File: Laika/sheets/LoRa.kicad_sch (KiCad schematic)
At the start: 0 parts

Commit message: Created schematic for Reyax RYLR993 LoRa module
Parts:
- added C13, C14: 47u, symbol Device:C
- added C15: 0.1u, symbol Device:C
- added C16: 100p, symbol Device:C
- added D16, D17, D18: LED, symbol Device:LED
- added J7: Conn_Coaxial_Small, symbol Connector:Conn_Coaxial_Small
- added JP1: SolderJumper_2_Open, symbol Jumper:SolderJumper_2_Open
- added Q5, Q6, Q7: Q_NMOS, symbol Device:Q_NMOS
- added R22, R23, R24, R25, R26, R27: 1k, symbol Device:R
- added TP6, TP7, TP8: TestPoint, TestPoint:TestPoint_Pad_D1.0mm, symbol Connector:TestPoint
- added U5: Reyax RYL993, Reyax_LoRa:RYLR993, symbol Reyax_LoRa:RYLR993
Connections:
- new net: Q6.D, R26.1
- new net: D17.1 (K), R26.2
- new net: Q6.G, R23.2
- new net: D16.1 (K), R25.2
- new net: D18.1 (K), R27.2
- new net: JP1.2 (B), U5.18 (PB12)
- new net: Q7.G, R24.2
- new net: Q5.G, R22.2
- new net: Q5.D, R25.1
- new net: Q7.D, R27.1
- new net +3V3: C13.1, C14.1, C15.1, C16.1, D16.2 (A), D17.2 (A), D18.2 (A), U5.12 (VBAT), U5.13 (VDD), U5.14 (VDD), U5.15 (VDD)
- new net GND: C13.2, C14.2, C15.2, C16.2, J7.2 (Ext), JP1.1 (A), Q5.S, Q6.S, Q7.S, U5.1 (GND), U5.10 (GND), U5.11 (GND), U5.22 (GND), U5.23 (GND), U5.28 (GND), U5.32 (GND), U5.41 (GND), U5.42 (GND), U5.44 (GND), U5.7 (GND), U5.8 (GND), U5.9 (GND)
- new net LINK: R22.1, U5.21 (PA12)
- new net LORA_ANTENNA: J7.1 (In), U5.43 (RF)
- new net LORA_NRST: TP8.1, U5.26 (NRST)
- new net LORA_RX: U5.40 (PA3/RXD)
- new net LORA_SWCLK: TP7.1, U5.27 (PA14/JTCK-SWCLK)
- new net LORA_SWDIO: TP6.1, U5.24 (PA13/JTMS-SWDIO)
- new net LORA_TX: U5.39 (PA2/TXD)
- new net RF_RX_ACTIVE: R24.1, U5.19 (PA10)
- new net RF_TX_ACTIVE: R23.1, U5.20 (PA11)
- no-connect marks 0 -> 17
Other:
- note added: "Antenna"
- note added: "LoRa Module"
- note added: "SWD"
- note added: "U.FL Connector"

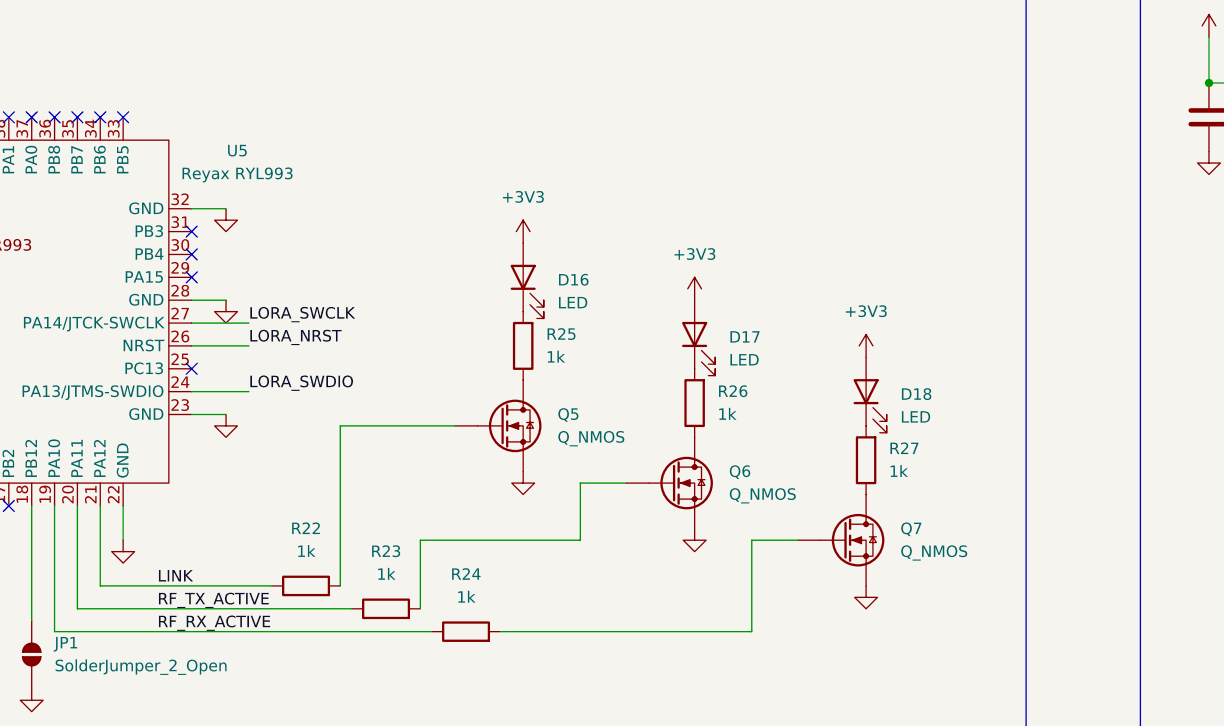
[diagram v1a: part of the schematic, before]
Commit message: Populated BOM with part numbers and footprints
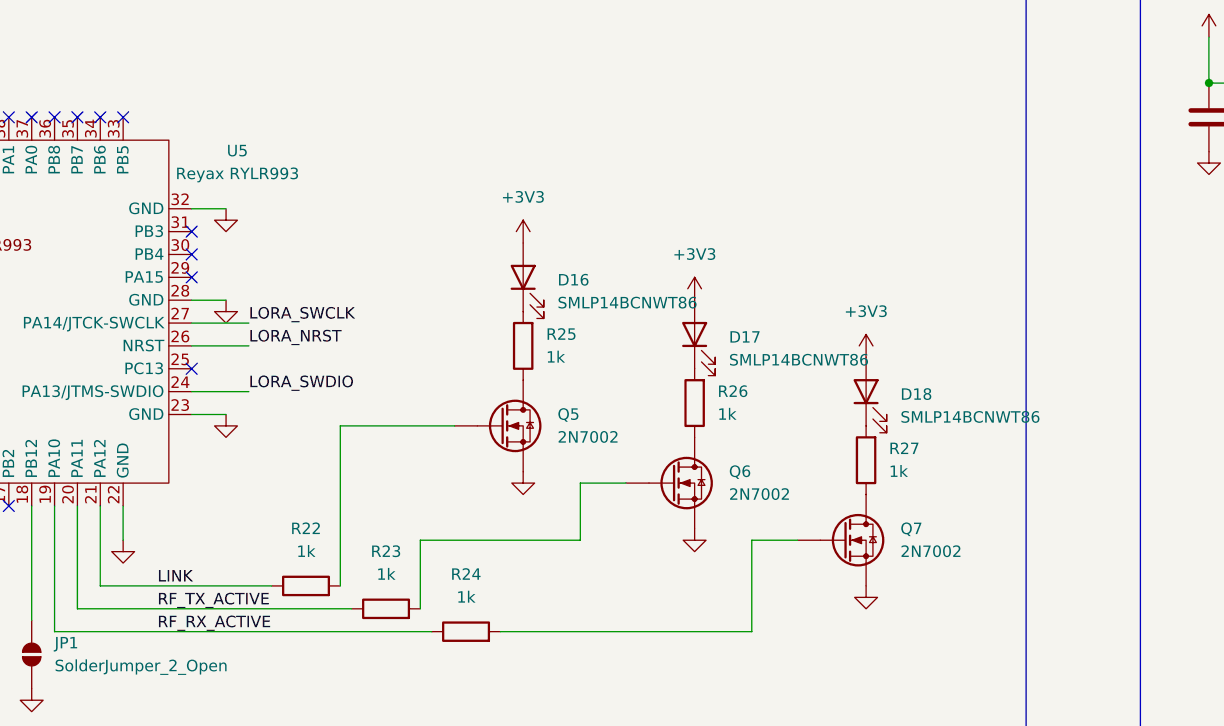
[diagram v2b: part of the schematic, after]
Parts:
- C13, C14: footprint (none) -> Capacitor_SMD:C_0805_2012Metric; JLC Part Type (none) -> Basic; Manafacturer (none) -> Samsung Electro-Mechanics; Part Number (none) -> CL21A476MQYNNNE
- C15: footprint (none) -> Capacitor_SMD:C_0402_1005Metric; JLC Part Type (none) -> Basic; Manafacturer (none) -> Samsung Electro-Mechanics; Part Number (none) -> CL05B104KO5NNNC
- C16: footprint (none) -> Capacitor_SMD:C_0201_0603Metric; JLC Part Type (none) -> Basic; Manafacturer (none) -> Samsung Electro-Mechanics; Part Number (none) -> CL10C101JB8NNNC
- D16, D17, D18: value LED -> SMLP14BCNWT86; footprint (none) -> LED_SMD:LED_0402_1005Metric; JLC Part Type (none) -> Extended; Manafacturer (none) -> Rohm Semiconductor; Part Number (none) -> SMLP14BCNWT86
- J7: footprint (none) -> Connector_Coaxial:U.FL_Molex_MCRF_73412-0110_Vertical; JLC Part Type (none) -> Extended; Manafacturer (none) -> Molex; Part Number (none) -> 0734120110
- JP1: footprint (none) -> Jumper:SolderJumper-2_P1.3mm_Open_Pad1.0x1.5mm
- Q5, Q6, Q7: value Q_NMOS -> 2N7002; footprint (none) -> Package_TO_SOT_SMD:SOT-23-3; JLC Part Type (none) -> Basic; Manafacturer (none) -> onsemi / Fairchild; Part Number (none) -> 2N7002
- R22, R23, R24, R25, R26, R27: footprint (none) -> Resistor_SMD:R_0402_1005Metric_Pad0.72x0.64mm_HandSolder; JLC Part Type (none) -> Basic; Manafacturer (none) -> Royalohm; Part Number (none) -> 0402WGF1001TCE
- U5: value Reyax RYL993 -> Reyax RYLR993; JLC Part Type (none) -> Extended; Manafacturer (none) -> REYAX; Part Number (none) -> RYLR993

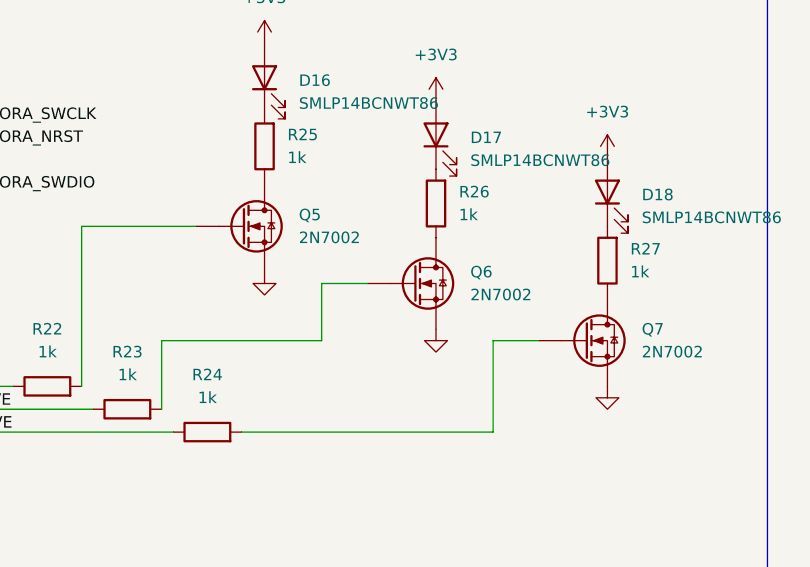
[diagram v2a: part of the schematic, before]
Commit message: Replace generic NMOS symbol with 2N7002
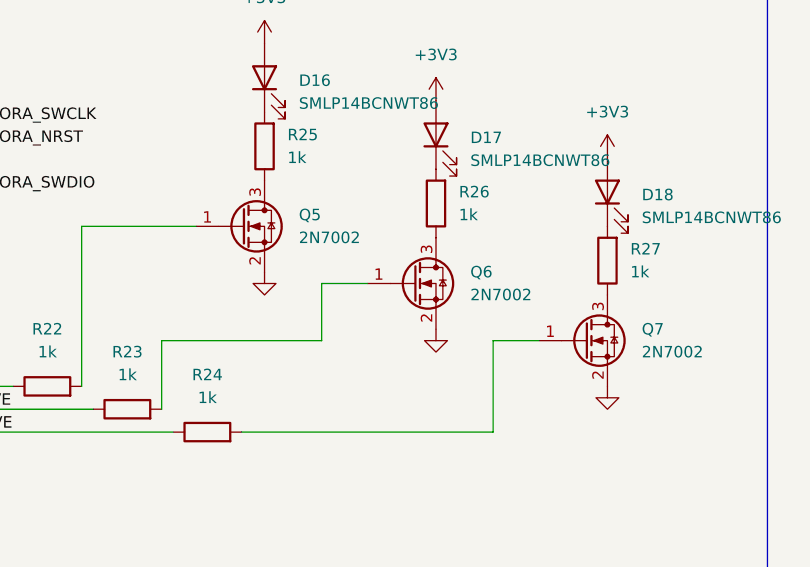
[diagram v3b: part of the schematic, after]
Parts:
- Q5, Q6, Q7: footprint Package_TO_SOT_SMD:SOT-23-3 -> Package_TO_SOT_SMD:SOT-23; symbol Device:Q_NMOS -> Transistor_FET:2N7002
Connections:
- net GND: now also Q5.2 (S), Q6.2 (S), Q7.2 (S); no longer Q5.S, Q6.S, Q7.S
- net at R26.1: now also Q6.3 (D); no longer Q6.D
- net at R23.2: now also Q6.1 (G); no longer Q6.G
- net at R24.2: now also Q7.1 (G); no longer Q7.G
- net at R22.2: now also Q5.1 (G); no longer Q5.G
- net at R25.1: now also Q5.3 (D); no longer Q5.D
- net at R27.1: now also Q7.3 (D); no longer Q7.D
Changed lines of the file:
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@@
 	)
 	(symbol
-		(lib_id "Device:Q_NMOS")
+		(lib_id "Transistor_FET:2N7002")
 		(at 151.13 107.95 0)
 		(unit 1)
@@
 			)
 		)
-		(property "Footprint" "Package_TO_SOT_SMD:SOT-23-3"
-			(at 156.21 105.41 0)
-			(effects
-				(font
-					(size 1.27 1.27)
-				)
-				(hide yes)
-			)
-		)
-		(property "Datasheet" "https://www.onsemi.com/download/data-sheet/pdf/nds7002a-d.pdf"
-			(at 151.13 107.95 0)
-			(effects
-				(font
-					(size 1.27 1.27)
-				)
-				(hide yes)
-			)
-		)
-		(property "Description" "N-MOSFET transistor"
+		(property "Footprint" "Package_TO_SOT_SMD:SOT-23"
+			(at 156.21 109.855 0)
+			(effects
+				(font
+					(size 1.27 1.27)
+					(italic yes)
+				)
+				(justify left)
+				(hide yes)
+			)
+		)
+		(property "Datasheet" "https://www.onsemi.com/pub/Collateral/NDS7002A-D.PDF"
+			(at 156.21 111.76 0)
+			(effects
+				(font
+					(size 1.27 1.27)
+				)
+				(justify left)
+				(hide yes)
+			)
+		)
+		(property "Description" "0.115A Id, 60V Vds, N-Channel MOSFET, SOT-23"
 			(at 151.13 107.95 0)
 			(effects
@@
 			)
 		)
-		(pin "S"
-		)
-		(pin "G"
-		)
-		(pin "D"
+		(pin "3"
+		)
+		(pin "1"
+		)
+		(pin "2"
 		)
 		(instances
@@
 	)
 	(symbol
-		(lib_id "Device:Q_NMOS")
+		(lib_id "Transistor_FET:2N7002")
 		(at 132.08 101.6 0)
 		(unit 1)
@@
 			)
 		)
-		(property "Footprint" "Package_TO_SOT_SMD:SOT-23-3"
-			(at 137.16 99.06 0)
-			(effects
-				(font
-					(size 1.27 1.27)
-				)
-				(hide yes)
-			)
-		)
-		(property "Datasheet" "https://www.onsemi.com/download/data-sheet/pdf/nds7002a-d.pdf"
-			(at 132.08 101.6 0)
-			(effects
-				(font
-					(size 1.27 1.27)
-				)
-				(hide yes)
-			)
-		)
-		(property "Description" "N-MOSFET transistor"
+		(property "Footprint" "Package_TO_SOT_SMD:SOT-23"
+			(at 137.16 103.505 0)
+			(effects
+				(font
+					(size 1.27 1.27)
+					(italic yes)
+				)
+				(justify left)
+				(hide yes)
+			)
+		)
+		(property "Datasheet" "https://www.onsemi.com/pub/Collateral/NDS7002A-D.PDF"
+			(at 137.16 105.41 0)
+			(effects
+				(font
+					(size 1.27 1.27)
+				)
+				(justify left)
+				(hide yes)
+			)
+		)
+		(property "Description" "0.115A Id, 60V Vds, N-Channel MOSFET, SOT-23"
 			(at 132.08 101.6 0)
 			(effects
@@
 			)
 		)
-		(pin "S"
-		)
-		(pin "G"
-		)
-		(pin "D"
+		(pin "1"
+		)
+		(pin "3"
+		)
+		(pin "2"
 		)
 		(instances
@@
 	)
 	(symbol
-		(lib_id "Device:Q_NMOS")
+		(lib_id "Transistor_FET:2N7002")
 		(at 170.18 114.3 0)
 		(unit 1)
@@
 			)
 		)
-		(property "Footprint" "Package_TO_SOT_SMD:SOT-23-3"
-			(at 175.26 111.76 0)
-			(effects
-				(font
-					(size 1.27 1.27)
-				)
-				(hide yes)
-			)
-		)
-		(property "Datasheet" "https://www.onsemi.com/download/data-sheet/pdf/nds7002a-d.pdf"
-			(at 170.18 114.3 0)
-			(effects
-				(font
-					(size 1.27 1.27)
-				)
-				(hide yes)
-			)
-		)
-		(property "Description" "N-MOSFET transistor"
+		(property "Footprint" "Package_TO_SOT_SMD:SOT-23"
+			(at 175.26 116.205 0)
+			(effects
+				(font
+					(size 1.27 1.27)
+					(italic yes)
+				)
+				(justify left)
+				(hide yes)
+			)
+		)
+		(property "Datasheet" "https://www.onsemi.com/pub/Collateral/NDS7002A-D.PDF"
+			(at 175.26 118.11 0)
+			(effects
+				(font
+					(size 1.27 1.27)
+				)
+				(justify left)
+				(hide yes)
+			)
+		)
+		(property "Description" "0.115A Id, 60V Vds, N-Channel MOSFET, SOT-23"
 			(at 170.18 114.3 0)
 			(effects
@@
 			)
 		)
-		(pin "S"
-		)
-		(pin "G"
-		)
-		(pin "D"
-		)
-		(instances
+		(pin "2"
+		)
+		(pin "1"
+		)
+		(pin "3"
+		)
+		(instances
